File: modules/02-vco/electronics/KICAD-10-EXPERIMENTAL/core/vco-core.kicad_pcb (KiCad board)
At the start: 2 copper layers, 58 x 110 mm, 146 parts, among them J1 Conn_01x04, J2 Conn_02x05_Odd_Even, J3 Conn_02x05_Odd_Even, J4 Conn_01x02, J5 Conn_02x03_Odd_Even, J6 Conn_02x02_Counter_Clockwise, J8 Conn_01x07, Q1 BC847BS, Q2 MMBT3906, Q3 J111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

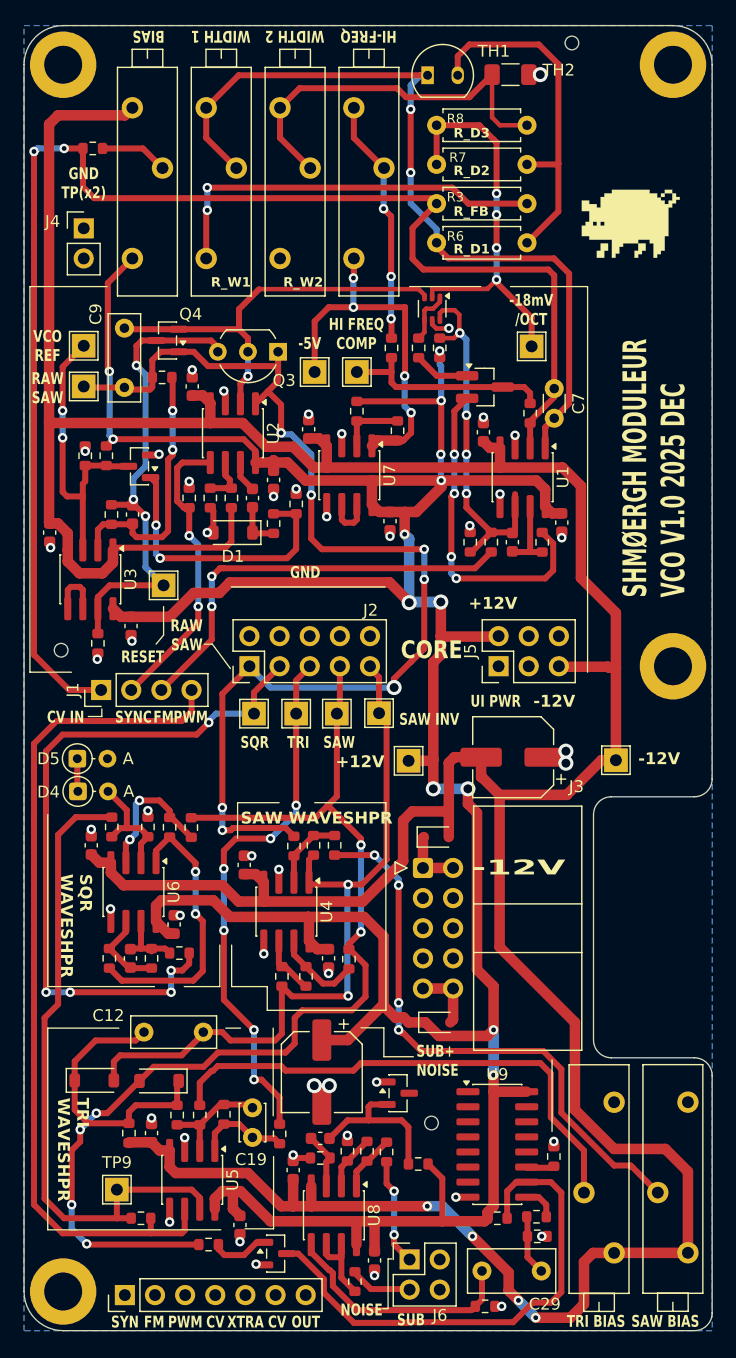
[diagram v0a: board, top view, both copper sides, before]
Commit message: Reverted VCO Core back to latest stable
- The latest working version of the VCO is this: (commit: https://github.com/shmoergh/moduleur/tree/b8f2f3887ee0ce40083da4d1238f04f5c6e473fa). Somewhere
between January 24 and May 24 the PCB got corrupted and it doesn't work properly. It could be the KiCAD 10 migration.
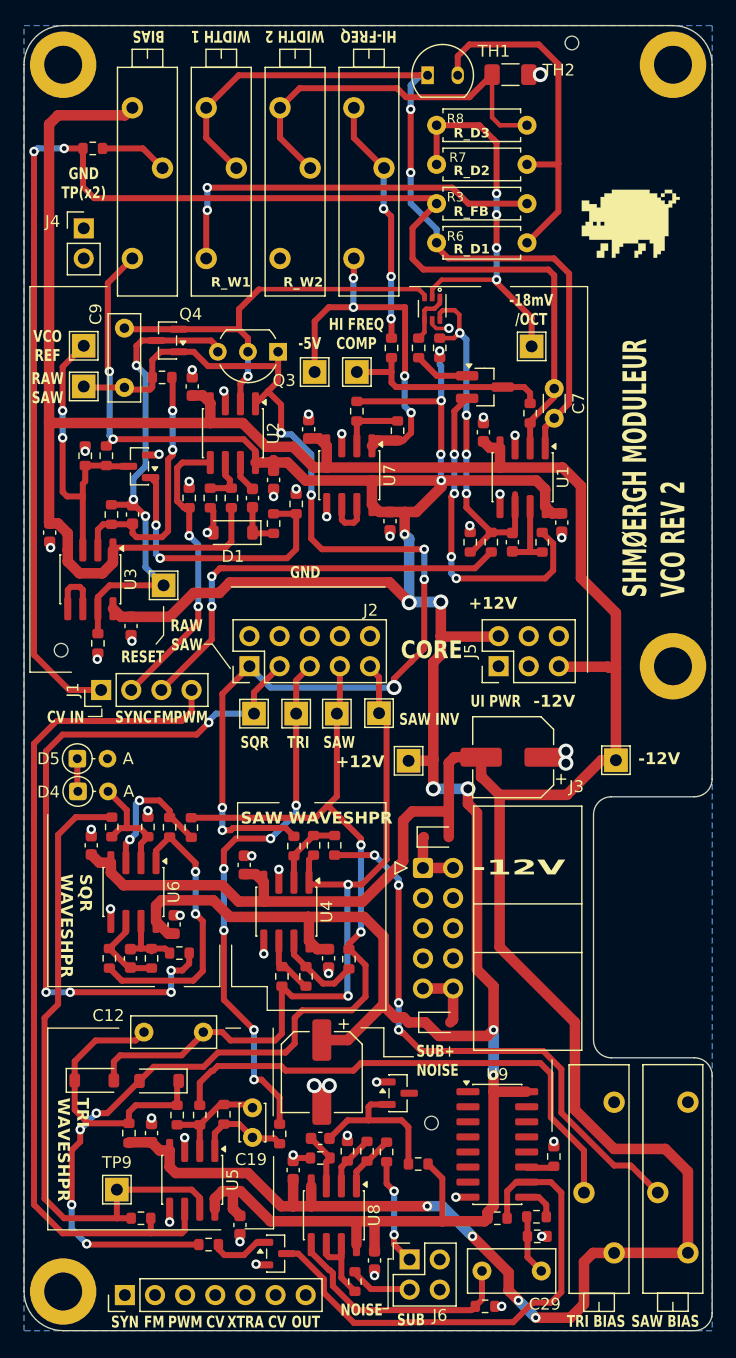
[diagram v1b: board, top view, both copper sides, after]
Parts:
- Q1: footprint Package_TO_SOT_SMD:SOT-363_SC-70-6 -> Shmoergh_Custom_Footprints:SOT-363_SC-70-6
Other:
- board text added: "SHMØERGH MODULEUR VCO REV 2"
- board text added: "VCO Core REV 1"
- board text removed: "SHMØERGH MODULEUR VCO V1.0 2025 DEC"
- board text removed: "SM-02 Analog VCO Core V1.0 / 2025 Dec"
